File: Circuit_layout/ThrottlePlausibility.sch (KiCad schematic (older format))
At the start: 56 parts, among them Q2 MMBF170, SW1 TS5A3159-Q1, U1 ACPL-C870, U15 LM339, U16 MCP6004, U2 LM7810CT, U3 LM7805CT, U4 MCP6004, U5 LM7332, U6 LM339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

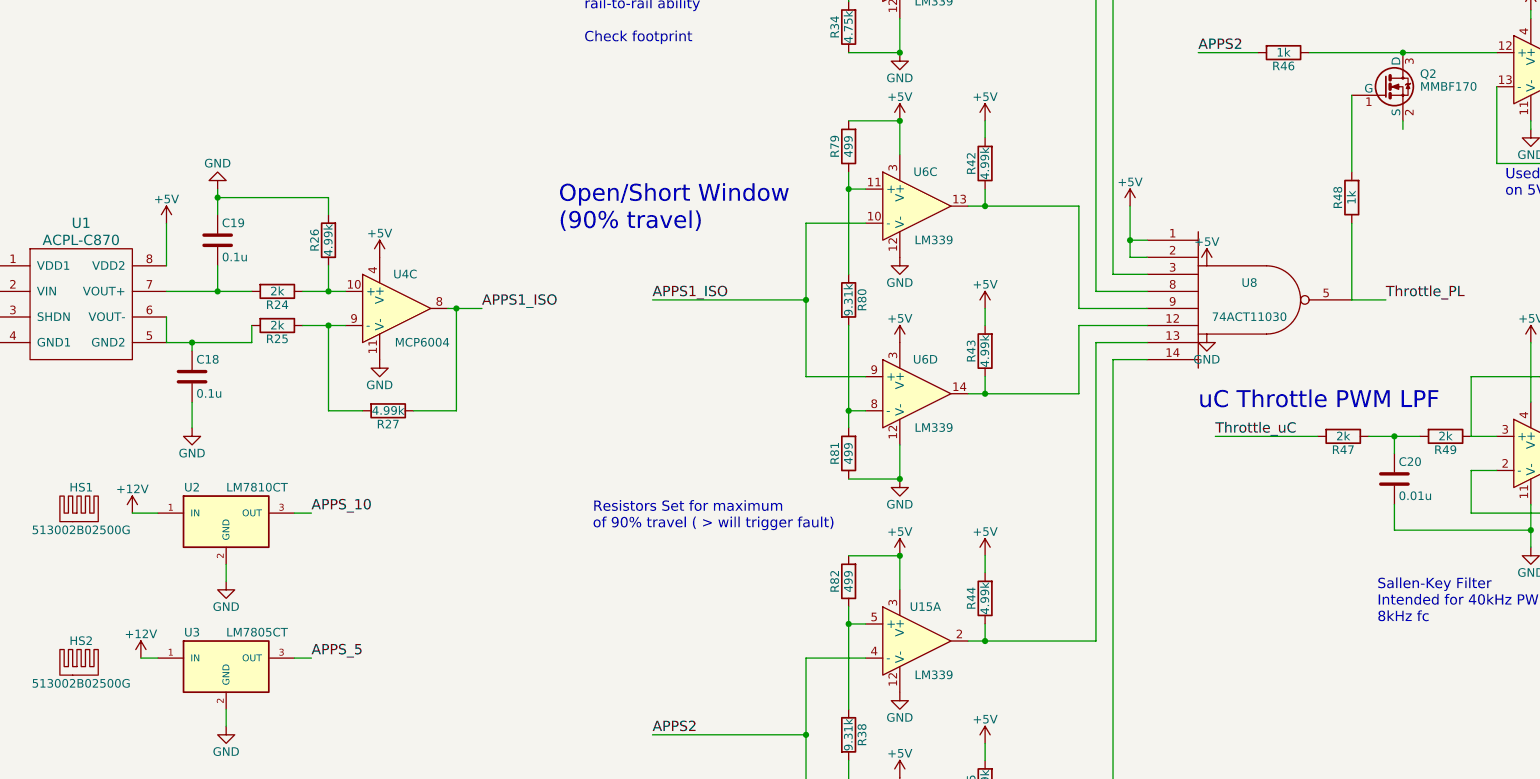
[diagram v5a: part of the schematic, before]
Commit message: eliminated warnings, need to clean things up + add footprints/datasheets
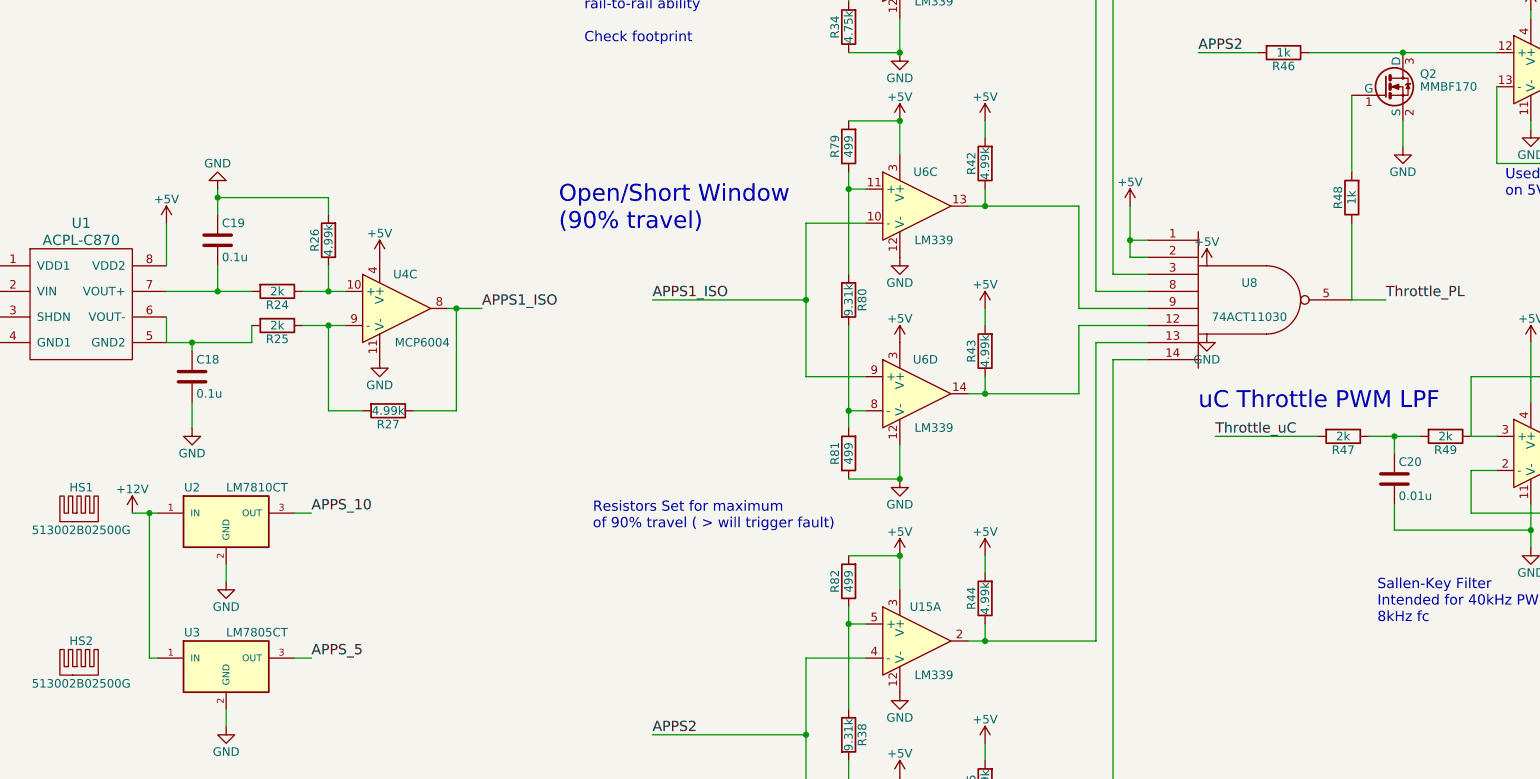
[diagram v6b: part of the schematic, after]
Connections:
- net GND: now also Q2.2 (S)

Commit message: cleaned up sch, added bypass pass. no net warnings
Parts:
- added C38, C39, C40, C41, C42, C43, C44, C45: 0.1u, Capacitors_SMD:C_0805_HandSoldering, symbol C
- renumbered U6 to U15, U16 to U4
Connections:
- net +12V: now also C12.1, C13.1
- net +5V: now also C38.1, C40.2, C41.1, C42.1, C43.1, C44.1, C45.1; no longer C13.1, C14.1, R23.1, U1.3 (SHDN), U1.4 (GND1), U3.3 (OUT)
- net APPS1: no longer C16.1, R29.2, R46.2, U15.4 (-), U15.7 (+)
- net APPS1_10: now also C17.1, C39.1; no longer C12.1
- net GND: now also C38.2, C40.1, C41.2, C42.2, C43.2, C44.2, C45.2
- net RTN_GLV: no longer C17.1
- new net +24V: C14.1
- new net APPS2: C16.1, R29.2, R46.2, U15.4 (-), U15.7 (+)
- new net APPS2_5: C39.2, R23.1, U1.3 (SHDN), U1.4 (GND1), U3.3 (OUT)
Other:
- moved on the sheet: C14, C15, C16, C18, C19, C20, C22, C24, HS1, HS2, Q2, R22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
